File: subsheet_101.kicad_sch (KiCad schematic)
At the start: 5 parts

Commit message: continue circuit vidéo
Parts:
- added C60: 100pF, symbol Device:C_Small
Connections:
- net GND: now also C60.2
- net ~{INILT}: now also C60.1
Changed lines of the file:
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@@
   (junction (at 82.55 52.07) (diameter 0) (color 0 0 0 0)
+  )
+  (junction (at 118.11 60.96) (diameter 0) (color 0 0 0 0)
   )
   (junction (at 82.55 41.91) (diameter 0) (color 0 0 0 0)
@@
     (stroke (width 0) (type default) (color 0 0 0 0))
   )
+  (wire (pts (xy 125.73 60.96) (xy 118.11 60.96))
+    (stroke (width 0) (type default) (color 0 0 0 0))
+  )
   (wire (pts (xy 59.69 64.77) (xy 59.69 71.12))
     (stroke (width 0) (type default) (color 0 0 0 0))
@@
     (stroke (width 0) (type default) (color 0 0 0 0))
   )
+  (wire (pts (xy 118.11 60.96) (xy 97.79 60.96))
+    (stroke (width 0) (type default) (color 0 0 0 0))
+  )
   (wire (pts (xy 85.09 64.77) (xy 85.09 71.12))
     (stroke (width 0) (type default) (color 0 0 0 0))
   )
-  (wire (pts (xy 95.25 63.5) (xy 95.25 71.12))
+  (wire (pts (xy 95.25 58.42) (xy 95.25 71.12))
     (stroke (width 0) (type default) (color 0 0 0 0))
   )
@@
     (stroke (width 0) (type default) (color 0 0 0 0))
   )
+  (wire (pts (xy 118.11 67.31) (xy 118.11 68.58))
+    (stroke (width 0) (type default) (color 0 0 0 0))
+  )
   (wire (pts (xy 125.73 116.84) (xy 132.08 116.84))
     (stroke (width 0) (type default) (color 0 0 0 0))
@@
     (stroke (width 0) (type default) (color 0 0 0 0))
   )
+  (wire (pts (xy 95.25 58.42) (xy 125.73 58.42))
+    (stroke (width 0) (type default) (color 0 0 0 0))
+  )
   (wire (pts (xy 35.56 129.54) (xy 41.91 129.54))
     (stroke (width 0) (type default) (color 0 0 0 0))
@@
     (stroke (width 0) (type default) (color 0 0 0 0))
   )
-  (wire (pts (xy 97.79 63.5) (xy 97.79 71.12))
+  (wire (pts (xy 97.79 60.96) (xy 97.79 71.12))
     (stroke (width 0) (type default) (color 0 0 0 0))
   )
@@
     (stroke (width 0) (type default) (color 0 0 0 0))
   )
+  (wire (pts (xy 118.11 60.96) (xy 118.11 62.23))
+    (stroke (width 0) (type default) (color 0 0 0 0))
+  )
   (wire (pts (xy 62.23 163.83) (xy 62.23 157.48))
     (stroke (width 0) (type default) (color 0 0 0 0))
@@
   )
   (wire (pts (xy 82.55 39.37) (xy 82.55 41.91))
+    (stroke (width 0) (type default) (color 0 0 0 0))
+  )
+  (wire (pts (xy 100.33 63.5) (xy 104.14 63.5))
     (stroke (width 0) (type default) (color 0 0 0 0))
   )
@@
     )
   )
-  (global_label "~{INILT}" (shape output) (at 97.79 63.5 90) (fields_autoplaced)
-    (effects (font (size 1.27 1.27)) (justify left))
-    (property "Intersheet References" "${INTERSHEET_REFS}" (id 0) (at 97.7106 56.5512 90)
-      (effects (font (size 1.27 1.27)) (justify left) hide)
-    )
-  )
-  (global_label "SYNLT" (shape output) (at 95.25 63.5 90) (fields_autoplaced)
-    (effects (font (size 1.27 1.27)) (justify left))
-    (property "Intersheet References" "${INTERSHEET_REFS}" (id 0) (at 95.1706 55.4626 90)
+  (global_label "~{INILT}" (shape output) (at 125.73 60.96 0) (fields_autoplaced)
+    (effects (font (size 1.27 1.27)) (justify left))
+    (property "Intersheet References" "${INTERSHEET_REFS}" (id 0) (at 132.6788 60.8806 0)
+      (effects (font (size 1.27 1.27)) (justify left) hide)
+    )
+  )
+  (global_label "SYNLT" (shape output) (at 125.73 58.42 0) (fields_autoplaced)
+    (effects (font (size 1.27 1.27)) (justify left))
+    (property "Intersheet References" "${INTERSHEET_REFS}" (id 0) (at 133.7674 58.3406 0)
       (effects (font (size 1.27 1.27)) (justify left) hide)
     )
@@
     )
   )
-  (global_label "~{SUPLT}" (shape output) (at 100.33 63.5 90) (fields_autoplaced)
-    (effects (font (size 1.27 1.27)) (justify left))
-    (property "Intersheet References" "${INTERSHEET_REFS}" (id 0) (at 100.2506 55.2812 90)
+  (global_label "~{SUPLT}" (shape output) (at 104.14 63.5 0) (fields_autoplaced)
+    (effects (font (size 1.27 1.27)) (justify left))
+    (property "Intersheet References" "${INTERSHEET_REFS}" (id 0) (at 112.3588 63.4206 0)
       (effects (font (size 1.27 1.27)) (justify left) hide)
     )
@@
     (pin "2")
   )
+  (symbol (lib_id "power:GND") (at 118.11 68.58 0) (unit 1)
+    (in_bom yes) (on_board yes)
+    (property "Reference" "#PWR?" (id 0) (at 118.11 74.93 0)
+      (effects (font (size 1.27 1.27)) hide)
+    )
+    (property "Value" "GND" (id 1) (at 119.38 71.12 0)
+      (effects (font (size 1.27 1.27)) (justify left))
+    )
+    (property "Footprint" "" (id 2) (at 118.11 68.58 0)
+      (effects (font (size 1.27 1.27)) hide)
+    )
+    (property "Datasheet" "" (id 3) (at 118.11 68.58 0)
+      (effects (font (size 1.27 1.27)) hide)
+    )
+    (pin "1")
+  )
   (symbol (lib_id "power:GND") (at 132.08 110.49 0) (unit 1)
     (in_bom yes) (on_board yes)
@@
     (pin "1")
   )
+  (symbol (lib_id "Device:C_Small") (at 118.11 64.77 0) (unit 1)
+    (in_bom yes) (on_board yes)
+    (property "Reference" "C60" (id 0) (at 119.38 63.5 0)
+      (effects (font (size 1.27 1.27)) (justify left))
+    )
+    (property "Value" "100pF" (id 1) (at 119.38 66.04 0)
+      (effects (font (size 1.27 1.27)) (justify left))
+    )
+    (property "Footprint" "" (id 2) (at 118.11 64.77 0)
+      (effects (font (size 1.27 1.27)) hide)
+    )
+    (property "Datasheet" "~" (id 3) (at 118.11 64.77 0)
+      (effects (font (size 1.27 1.27)) hide)
+    )
+    (pin "1")
+    (pin "2")
+  )
   (symbol (lib_id "Device:R_Small") (at 162.56 97.79 0) (unit 1)

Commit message: ports d'extension et cartouche
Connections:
- net SYNLT renamed A/SYNLT
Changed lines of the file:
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@@
     )
   )
-  (global_label "SYNLT" (shape output) (at 125.73 58.42 0) (fields_autoplaced)
+  (global_label "A{slash}SYNLT" (shape output) (at 125.73 58.42 0) (fields_autoplaced)
     (effects (font (size 1.27 1.27)) (justify left))
-    (property "Intersheet References" "${INTERSHEET_REFS}" (id 0) (at 133.7674 58.3406 0)
+    (property "Intersheet References" "${INTERSHEET_REFS}" (id 0) (at 136.1864 58.3406 0)
       (effects (font (size 1.27 1.27)) (justify left) hide)
     )

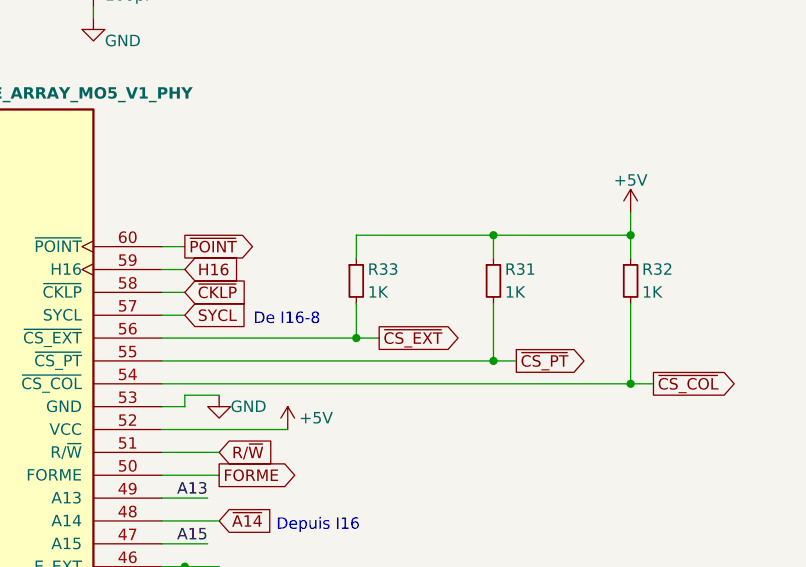
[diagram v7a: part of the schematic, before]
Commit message: fixes DRC : duplicate, designators with '?'
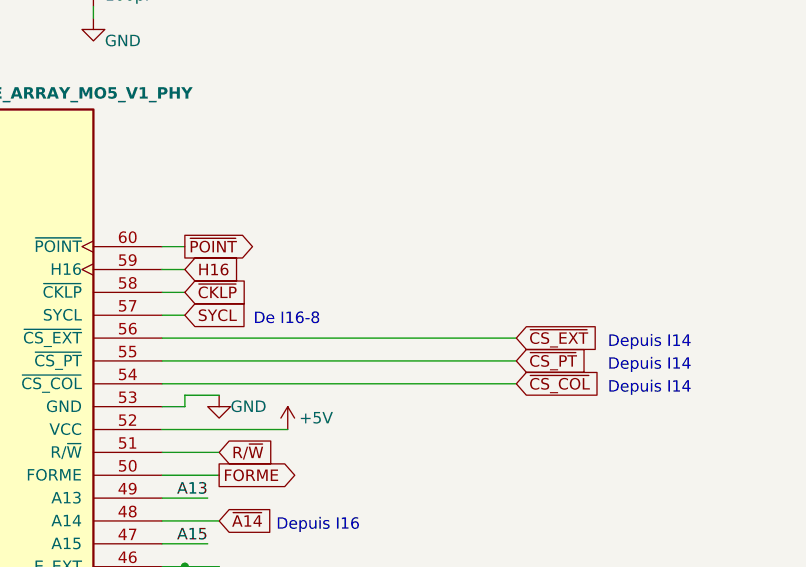
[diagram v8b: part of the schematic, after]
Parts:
- removed R31, R32, R33: 1K, symbol Device:R_Small
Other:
- note added: "Depuis I14"
